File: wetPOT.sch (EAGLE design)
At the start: 2 parts

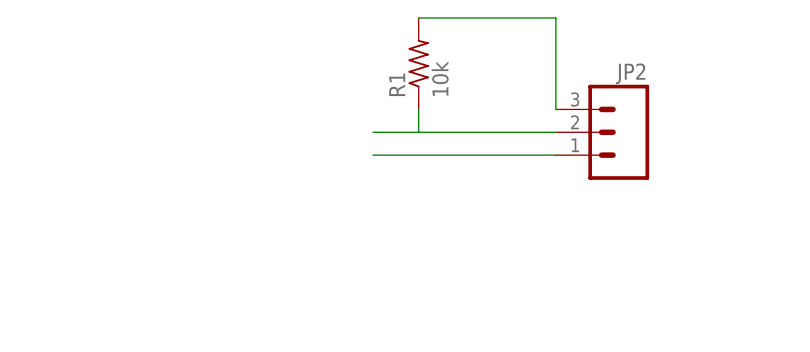
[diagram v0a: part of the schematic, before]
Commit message: Updated resistor to correct form factor.
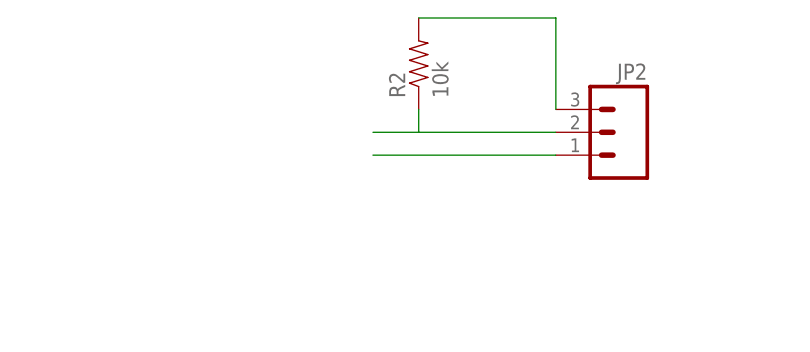
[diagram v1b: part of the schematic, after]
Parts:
- removed R1: 10k, resistor:R-US_0204/5
- added R2: 10k, SparkFun-Resistors:10KOHM-1/4W-1%(PTH)HORIZ
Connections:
- net PIN0: now also R2.2; no longer R1.2
- net PIN1: now also R2.1; no longer R1.1
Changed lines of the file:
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@@
 <layer number="223" name="223bmp" color="24" fill="1" visible="no" active="no"/>
 <layer number="224" name="224bmp" color="25" fill="1" visible="no" active="no"/>
+<layer number="225" name="225bmp" color="7" fill="1" visible="yes" active="yes"/>
+<layer number="226" name="226bmp" color="7" fill="1" visible="yes" active="yes"/>
+<layer number="227" name="227bmp" color="7" fill="1" visible="yes" active="yes"/>
+<layer number="228" name="228bmp" color="7" fill="1" visible="yes" active="yes"/>
+<layer number="229" name="229bmp" color="7" fill="1" visible="yes" active="yes"/>
+<layer number="230" name="230bmp" color="7" fill="1" visible="yes" active="yes"/>
+<layer number="231" name="231bmp" color="7" fill="1" visible="yes" active="yes"/>
 <layer number="248" name="Housing" color="7" fill="1" visible="yes" active="yes"/>
 <layer number="249" name="Edge" color="7" fill="1" visible="yes" active="yes"/>
@@
 <parts>
 <part name="FRAME2" library="frames" deviceset="LETTER_L" device=""/>
-<part name="R1" library="resistor" deviceset="R-US_" device="0204/5" value="10k"/>
 <part name="JP2" library="SparkFun-Connectors" deviceset="M03" device="PTH"/>
+<part name="R2" library="SparkFun-Resistors" deviceset="10KOHM-1/4W-1%(PTH)" device="HORIZ" value="10k"/>
 </parts>
 <sheets>
@@
 <instance part="FRAME2" gate="G$1" x="0" y="0"/>
 <instance part="FRAME2" gate="G$2" x="147.32" y="0"/>
-<instance part="R1" gate="G$1" x="203.2" y="101.6" rot="R90"/>
 <instance part="JP2" gate="G$1" x="226.06" y="93.98" rot="MR0"/>
+<instance part="R2" gate="G$1" x="203.2" y="101.6" rot="R90"/>
 </instances>
 <busses>
@@
 <net name="PIN0" class="0">
 <segment>
-<pinref part="R1" gate="G$1" pin="2"/>
 <pinref part="JP2" gate="G$1" pin="3"/>
+<wire x1="218.44" y1="106.68" x2="218.44" y2="96.52" width="0.1524" layer="91"/>
+<pinref part="R2" gate="G$1" pin="2"/>
 <wire x1="203.2" y1="106.68" x2="218.44" y2="106.68" width="0.1524" layer="91"/>
-<wire x1="218.44" y1="106.68" x2="218.44" y2="96.52" width="0.1524" layer="91"/>
 </segment>
 </net>
 <net name="PIN1" class="0">
 <segment>
-<pinref part="R1" gate="G$1" pin="1"/>
 <wire x1="198.12" y1="93.98" x2="203.2" y2="93.98" width="0.1524" layer="91"/>
 <wire x1="203.2" y1="96.52" x2="203.2" y2="93.98" width="0.1524" layer="91"/>
 <pinref part="JP2" gate="G$1" pin="2"/>
 <wire x1="203.2" y1="93.98" x2="218.44" y2="93.98" width="0.1524" layer="91"/>
+<pinref part="R2" gate="G$1" pin="1"/>
 </segment>
 </net>

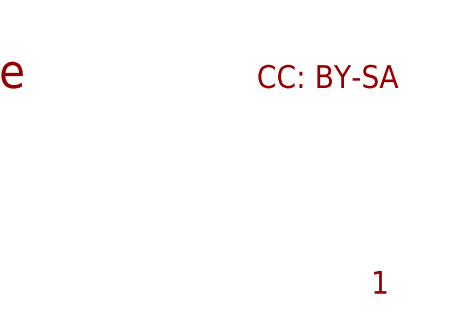
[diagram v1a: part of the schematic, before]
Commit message: Updated rev number on silkscreen and board layout.
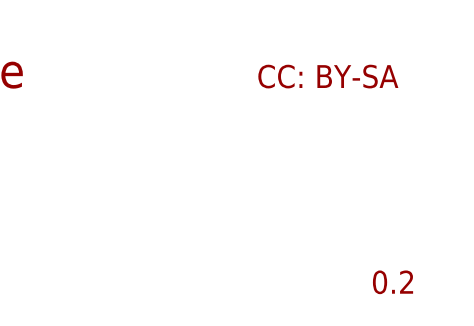
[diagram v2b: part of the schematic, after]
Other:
- note added: "0.2"
- note removed: "1"
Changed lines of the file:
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@@
 <text x="149.86" y="25.4" size="2.1844" layer="94">Andrew S. Parnell</text>
 <text x="228.6" y="30.48" size="2.54" layer="94">CC: BY-SA</text>
-<text x="241.3" y="7.62" size="2.54" layer="94">1</text>
+<text x="241.3" y="7.62" size="2.54" layer="94">0.2</text>
 </plain>
 <instances>
